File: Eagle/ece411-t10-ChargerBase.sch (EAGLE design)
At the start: 51 parts, among them IC1 NE5532D, IC2 TINY24/44/84-SSU, IC3 NE5532D, IC5 AZ1117IH-5.0V, Q1 2N3906, T1 2N3904, T2 2N3904, T3 2N3904

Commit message: Boards + schematics rev2
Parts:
- removed C12, C2: 100n, rcl:C-USC0805
- removed C3, C4, C5, C6: 1nF, rcl:C-EUC0805
- removed C7: 1uF, adafruit:C-US050-025X075
- removed C8: 10nF, adafruit:C-US050-025X075
- removed C9: 100n, rcl:C-EUC0805
- removed D1: 1N4004, adafruit:1N4004
- removed IC1, IC3: NE5532D, linear:NE5532D
- removed Q1: 2N3906, transistor-pnp:2N3906
- removed R18, R19: 10k, rcl:R-US_R0805
- removed R3, R4, R5, R6, R7, R8, R9: 1k, rcl:R-US_R0805
- removed T2: 2N3904, transistor:2N3904
- removed TM1: 100k, adafruit:TRIMPOTTC33X
- added Q1-NP, Q2-NP, Q3-NP, Q4, Q5-NP: NP, transistor-fet:TN0602N3
- added Q6: RFD16N05LSM9ACTTO252, _VMS:RFD16N05LSM9ACTTO252
- R1: value 1k -> 0R
- R12, R17: value 1k -> 5k
- S1, S2: value REED-SWITCH-MK6-6 -> REED-SWITCH
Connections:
- removed net COIL_DRIVER: C6.2, C9.1, IC3B.OUT, R6.1
- removed net N$1: C3.1, IC1A.+IN, R1.1, R3.2
- removed net N$10: C4.2, IC1B.OUT, R4.1, R8.2
- removed net N$11: C5.1, IC3A.+IN, R5.2, R8.1
- removed net N$12: C5.2, IC3A.OUT, R5.1, R9.2
- removed net N$13: C6.1, IC3B.+IN, R6.2, R9.1
- removed net N$15: IC3B.-IN, TM1.S
- removed net N$27: C7.1, Q1.E, T2.E
- removed net N$28: C9.2, D1.A, R18.1, T2.B
- removed net N$29: D1.C, Q1.B, R19.2
- removed net N$30: C7.2, C8.1, TX_COIL-1.S
- removed net N$8: C3.2, IC1A.OUT, R3.1, R7.2
- removed net N$9: C4.1, IC1B.+IN, R4.2, R7.1
- new net DRAIN: Q1-NP.D, Q2-NP.D, Q3-NP.D, Q4.D, Q5-NP.D, Q6.D, TX_COIL-2.S
- net GND: now also Q1-NP.S, Q2-NP.S, Q3-NP.S, Q4.S, Q5-NP.S, Q6.S; no longer C12.2, C2.2, C8.2, IC1A.-IN, IC1B.-IN, IC1P.V-, IC3A.-IN, IC3P.V-, Q1.C, R19.1, TM1.A, TX_COIL-2.S
- net MOSI: now also R1.2
- net PWM: now also Q1-NP.G, Q2-NP.G, Q3-NP.G, Q4.G, Q5-NP.G, Q6.G, R1.1; no longer IC2.(PCINT7/ICP/OC0B/ADC7)PA7, R1.2
- net VDD: now also TX_COIL-1.S; no longer C12.1, C2.1, IC1P.V+, IC3P.V+, R18.2, T2.C, TM1.E
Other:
- note added: "*place either the one T0-252 MOSFET, or TO-92 MOSFET x 5"
- note added: "*place one or the other"
- note removed: "Filtering"
- note removed: "Offset and Gain"
- note removed: "Signal conditioning stage"
- moved on the sheet: R1, R12, R17, TX_COIL-1, TX_COIL-2

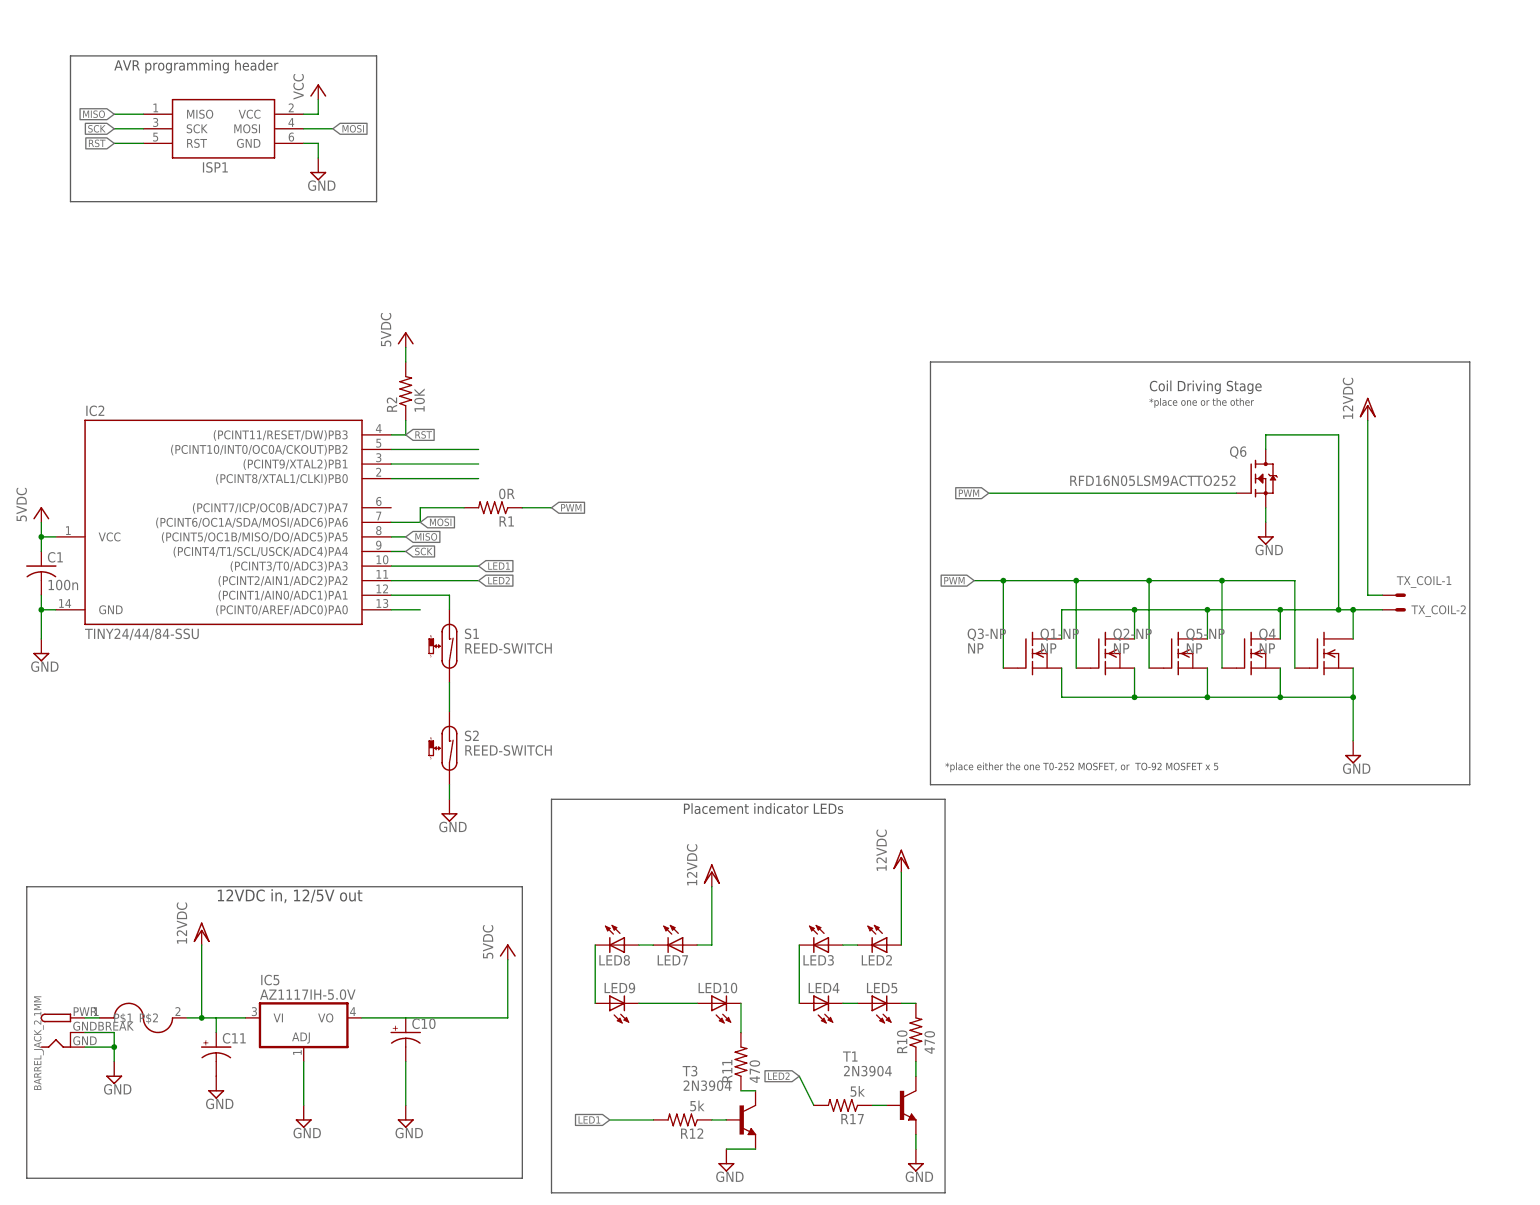
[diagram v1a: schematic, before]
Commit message: cleaned up schematic. fixed minor ERC error
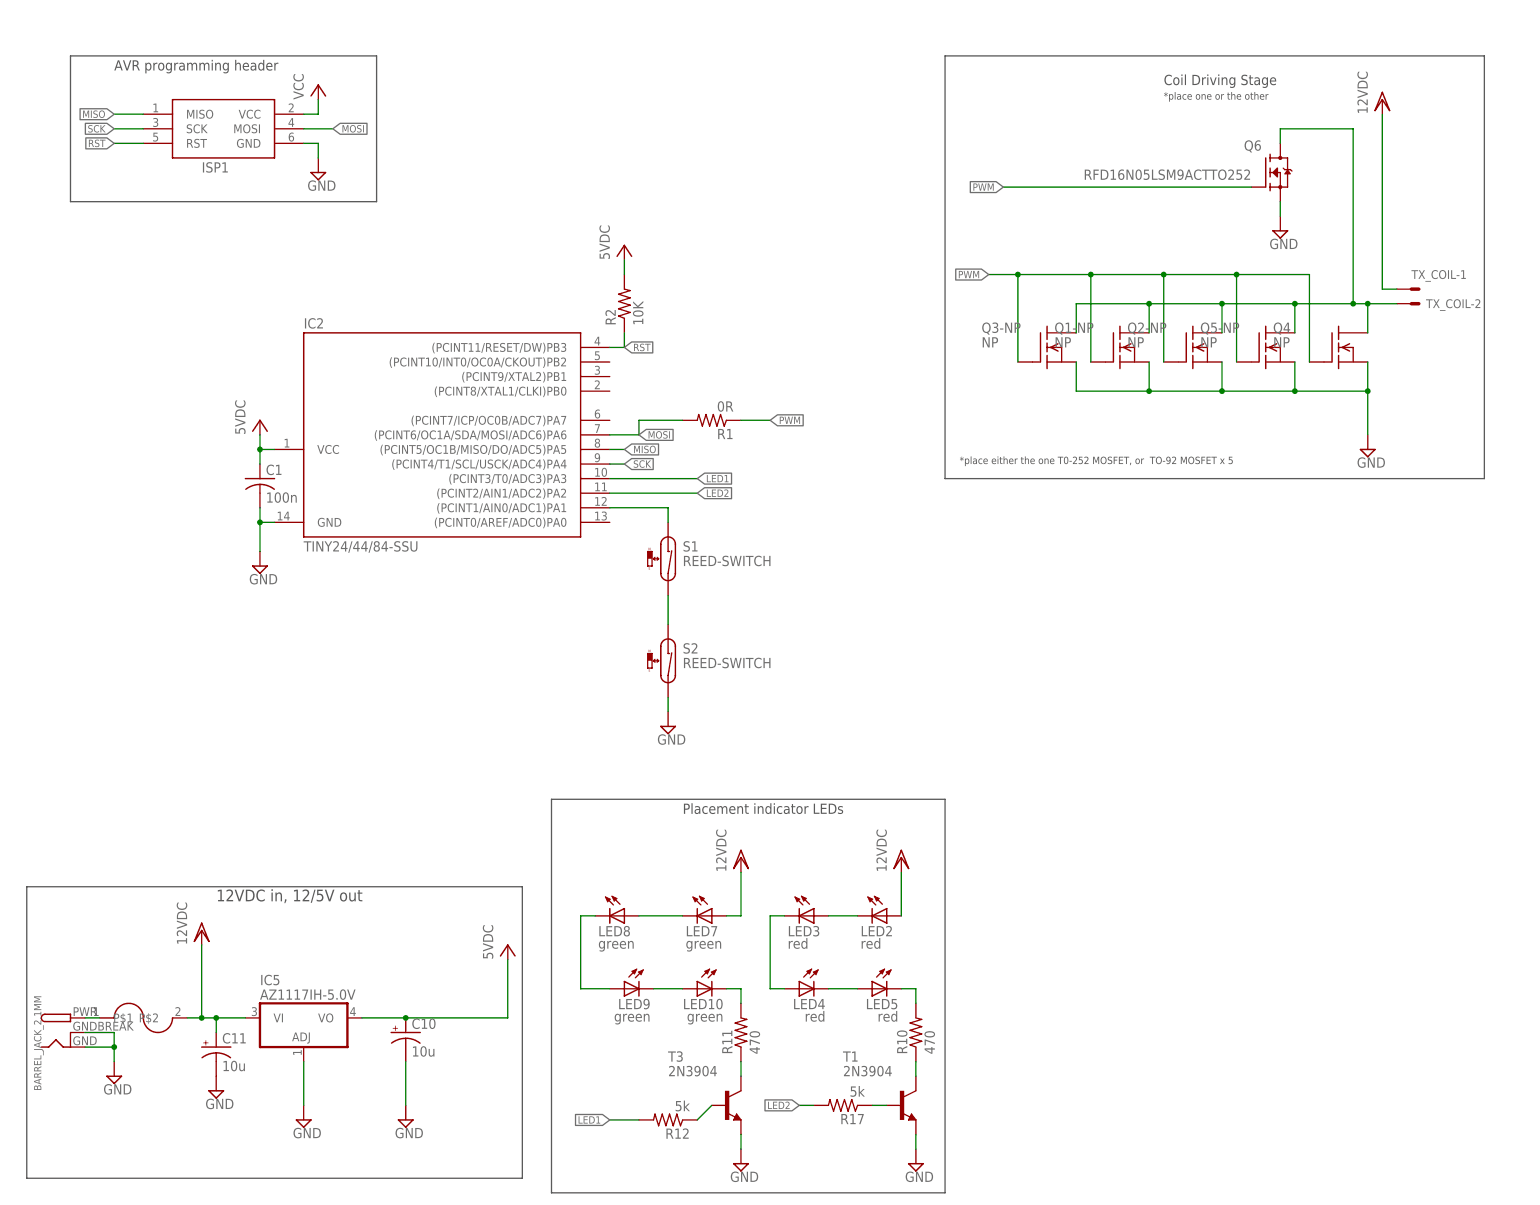
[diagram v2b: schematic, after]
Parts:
- C10, C11: value (none) -> 10u
- LED10, LED7, LED8, LED9: value (none) -> green
- LED2, LED3, LED4, LED5: value (none) -> red
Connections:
- removed net N$3: IC2.(PCINT8/XTAL1/CLKI)PB0
- removed net N$4: IC2.(PCINT9/XTAL2)PB1
- removed net N$5: IC2.(PCINT10/INT0/OC0A/CKOUT)PB2
- removed net PIN13: IC2.(PCINT0/AREF/ADC0)PA0
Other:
- moved on the sheet: C1, IC2, LED10, LED2, LED3, LED4, LED5, LED7, LED8, LED9, Q1-NP, Q2-NP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

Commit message: clean up
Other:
- moved on the sheet: IC5
